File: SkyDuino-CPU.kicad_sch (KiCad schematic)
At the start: 35 parts, among them J11 USB-A RMT, J8 DBG, J9 USB_C Artisan, SW1 BOOT, U6 STM32F411RET6, U7 25MHz, U8 USBLC6-2SC6, U9 USBLC6-2SC6, Y1 32.768kHz

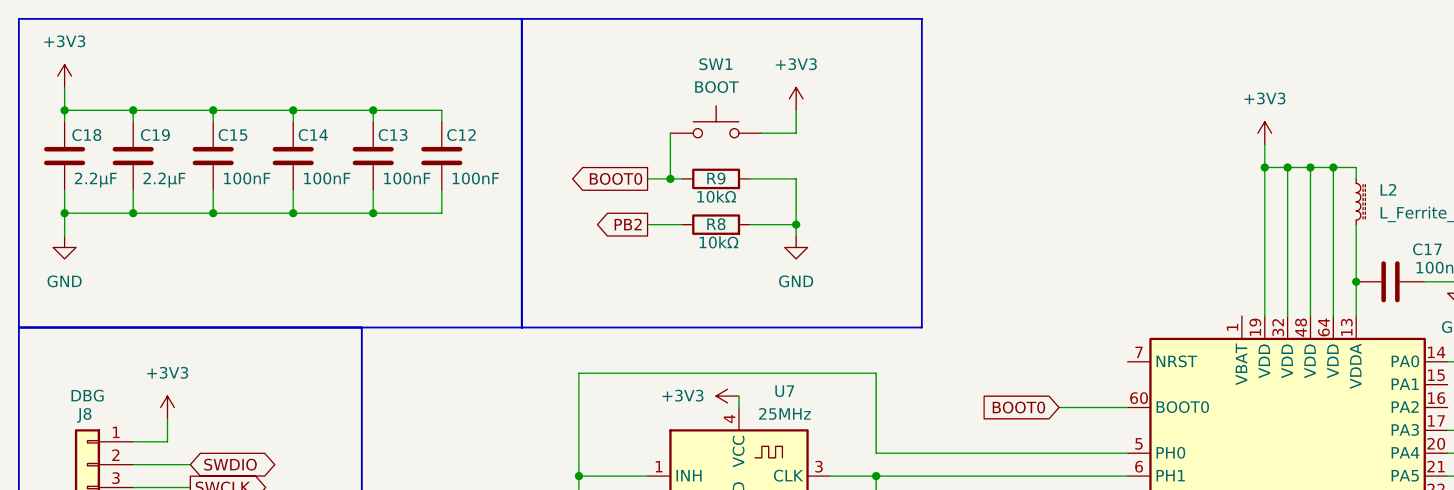
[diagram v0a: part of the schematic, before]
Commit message: Add VBat to VDD
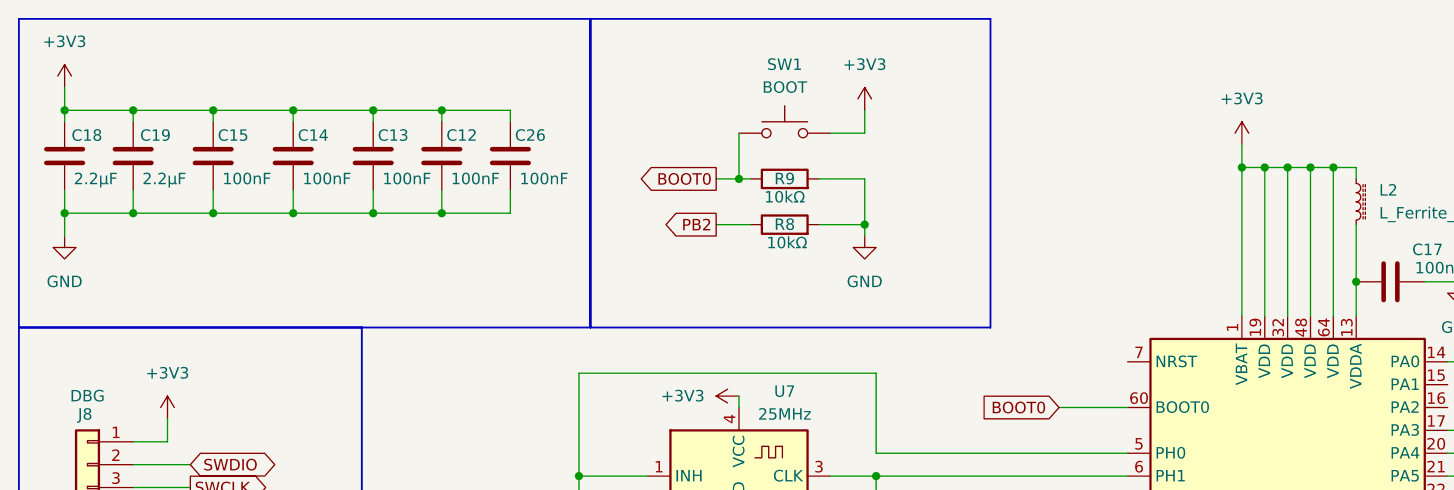
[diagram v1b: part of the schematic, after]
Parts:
- added C26: 100nF, Capacitor_SMD:C_0805_2012Metric_Pad1.18x1.45mm_HandSolder, symbol Device:C
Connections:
- net +3V3: now also U6.1 (VBAT), C26.1
- net GND: now also C26.2
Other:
- moved on the sheet: R8, R9, SW1

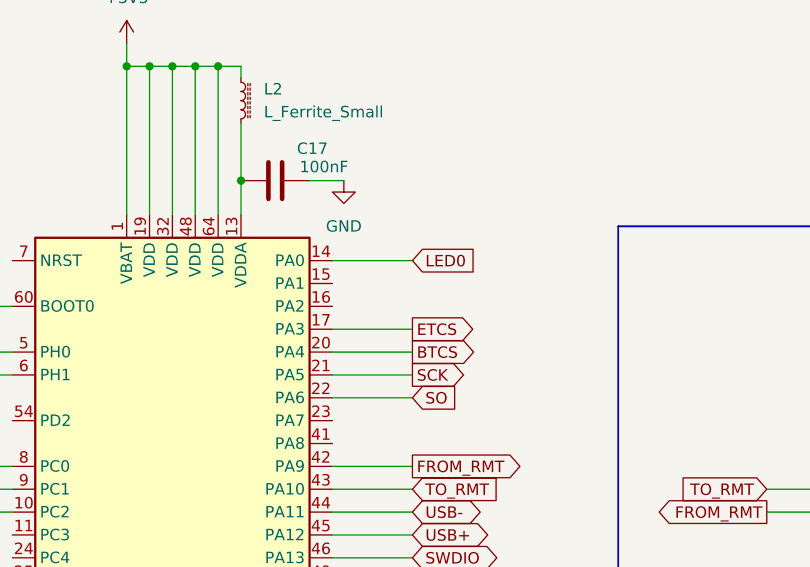
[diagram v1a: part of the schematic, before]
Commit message: Add NTC connection
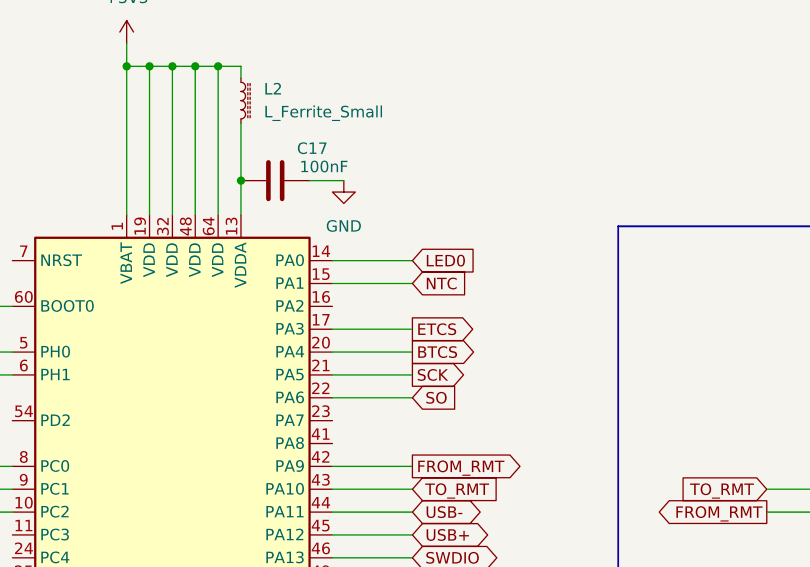
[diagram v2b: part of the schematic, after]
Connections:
- net NTC: now reaches U6.15 (PA1)
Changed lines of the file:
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@@
+	(wire
+		(pts
+			(xy 171.45 54.61) (xy 180.34 54.61)
+		)
+		(stroke
+			(width 0)
+			(type default)
+		)
+	)
 	(wire
 		(pts
@@
 				(hide yes)
 			)
+		)
+	)
+	(global_label "NTC"
+		(shape input)
+		(at 180.34 54.61 0)
+		(fields_autoplaced yes)
+		(effects
+			(font
+				(size 1.27 1.27)
+			)
+			(justify left)
+		)
+		(property "Intersheetrefs" "${INTERSHEET_REFS}"
+			(at 186.8933 54.61 0)
+			(effects
+				(font
+					(size 1.27 1.27)
+				)
+				(justify left)
+				(hide yes)
+			)

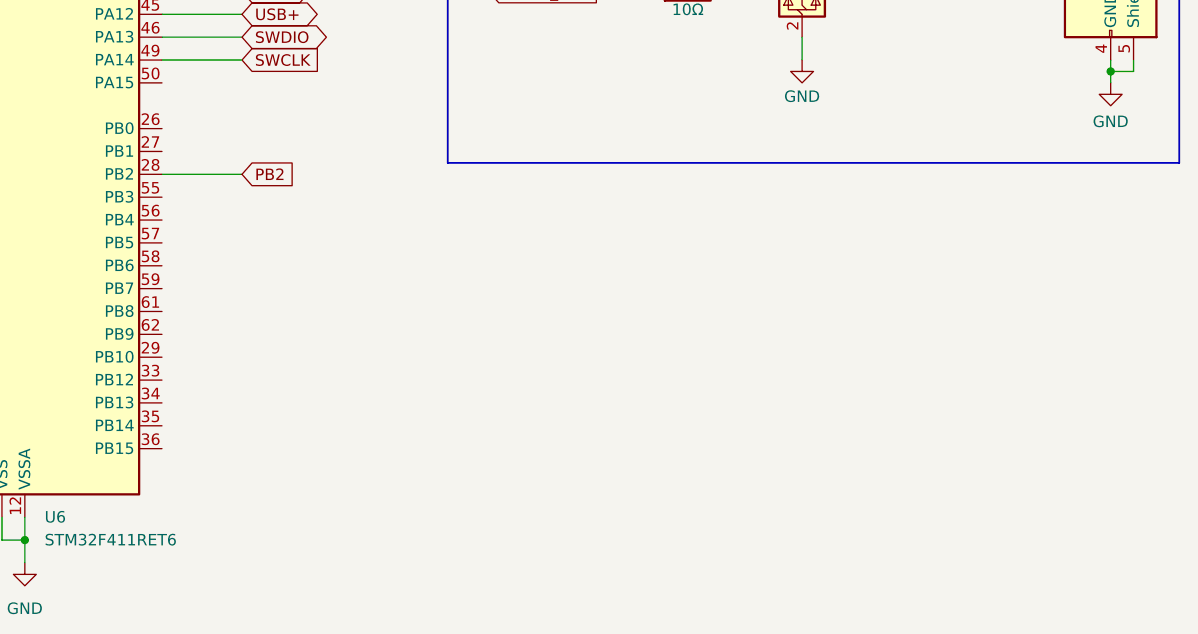
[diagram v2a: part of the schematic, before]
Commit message: Add I2C for the display
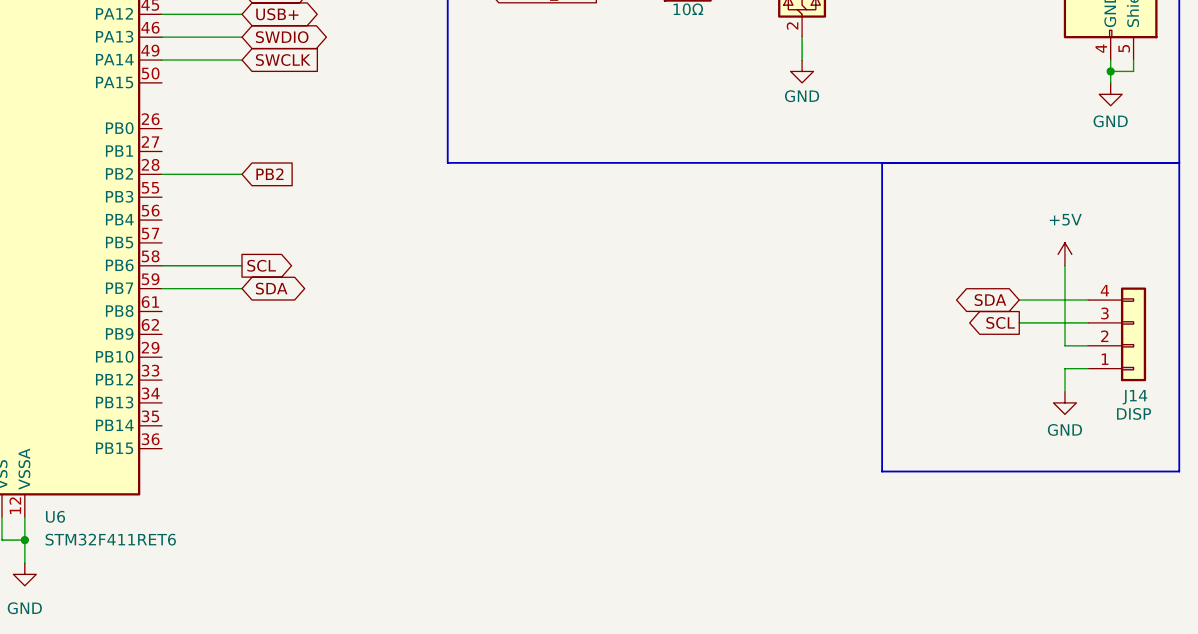
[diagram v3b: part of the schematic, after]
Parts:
- added J14: DISP, Connector_PinHeader_2.54mm:PinHeader_1x04_P2.54mm_Vertical, symbol Connector_Generic:Conn_01x04
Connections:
- net +5V: now also J14.2 (Pin_2)
- net GND: now also J14.1 (Pin_1)
- net SCL: now reaches U6.58 (PB6)
- net SCL: now also J14.3 (Pin_3)
- net SDA: now reaches U6.59 (PB7)
- net SDA: now also J14.4 (Pin_4)

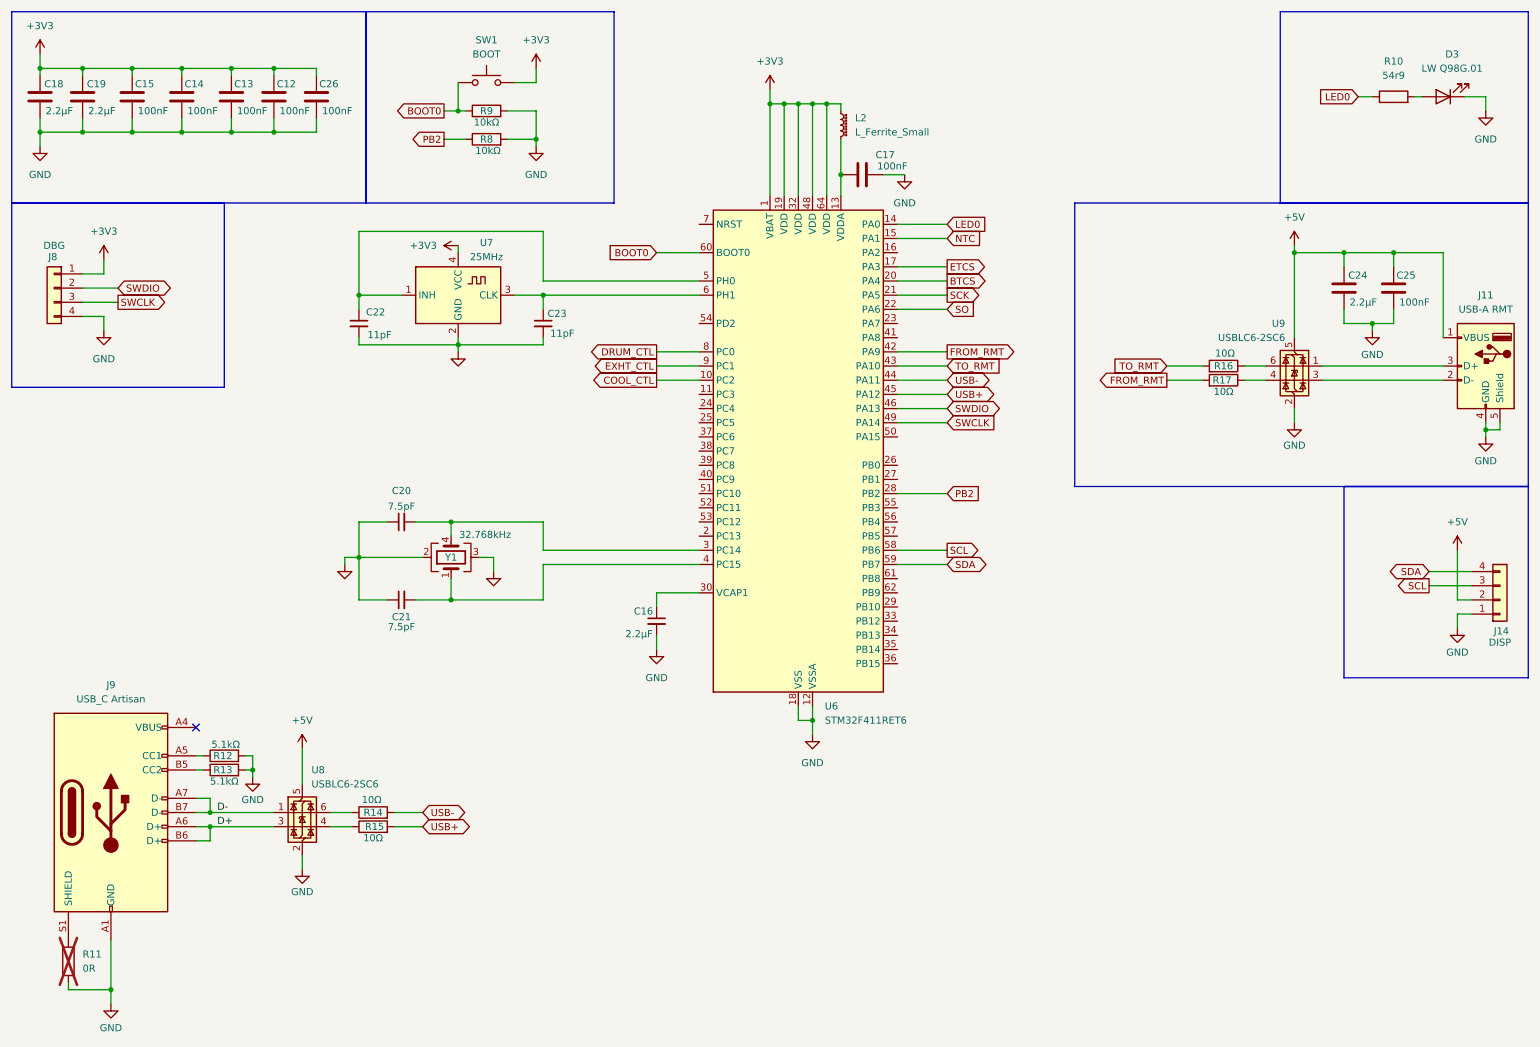
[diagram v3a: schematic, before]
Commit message: Re-annotate. Add NTC capacitor
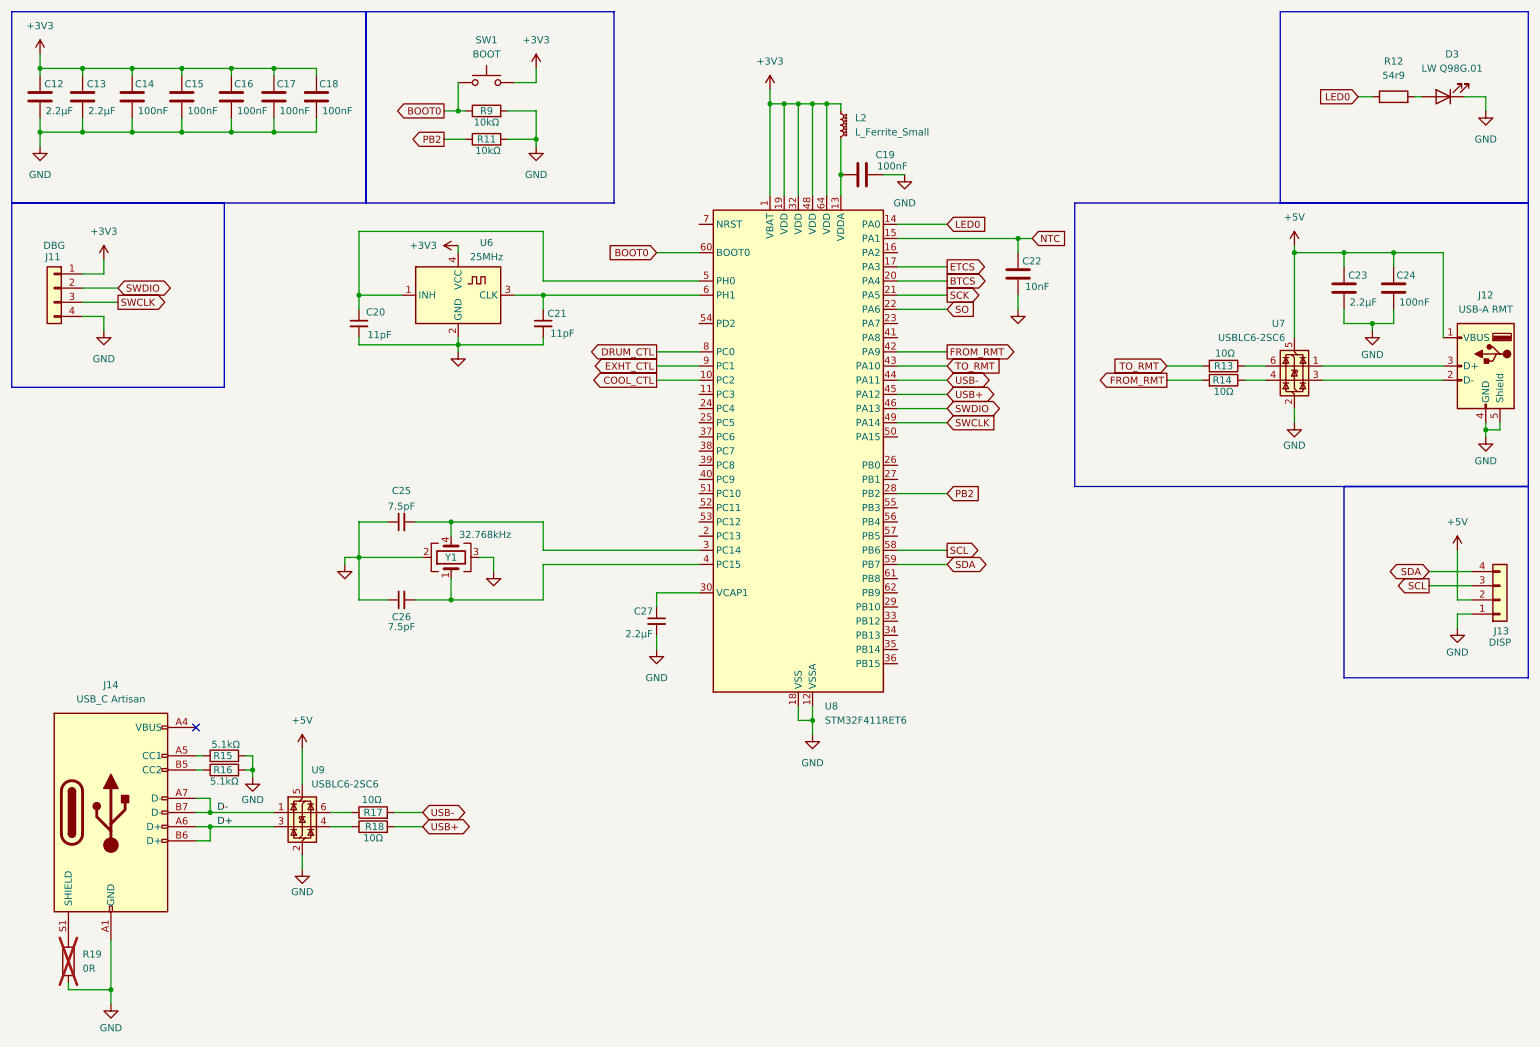
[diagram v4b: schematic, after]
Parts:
- added C22: 10nF, Capacitor_SMD:C_0805_2012Metric_Pad1.18x1.45mm_HandSolder, symbol Device:C
- renumbered C18 to C12, C19 to C13, C15 to C14, C14 to C15, C13 to C16, C12 to C17, C26 to C18, C17 to C19, C22 to C20, C23 to C21, C24 to C23, C25 to C24, C20 to C25, C21 to C26, C16 to C27, J8 to J11, J11 to J12, J14 to J13, J9 to J14, R8 to R11, R10 to R12, R16 to R13, R17 to R14, R12 to R15, R13 to R16, R14 to R17, R15 to R18, R11 to R19, U7 to U6, U9 to U7, U6 to U8, U8 to U9
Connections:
- net GND: now also C22.2
- net NTC: now also C22.1

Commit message: Add SSR
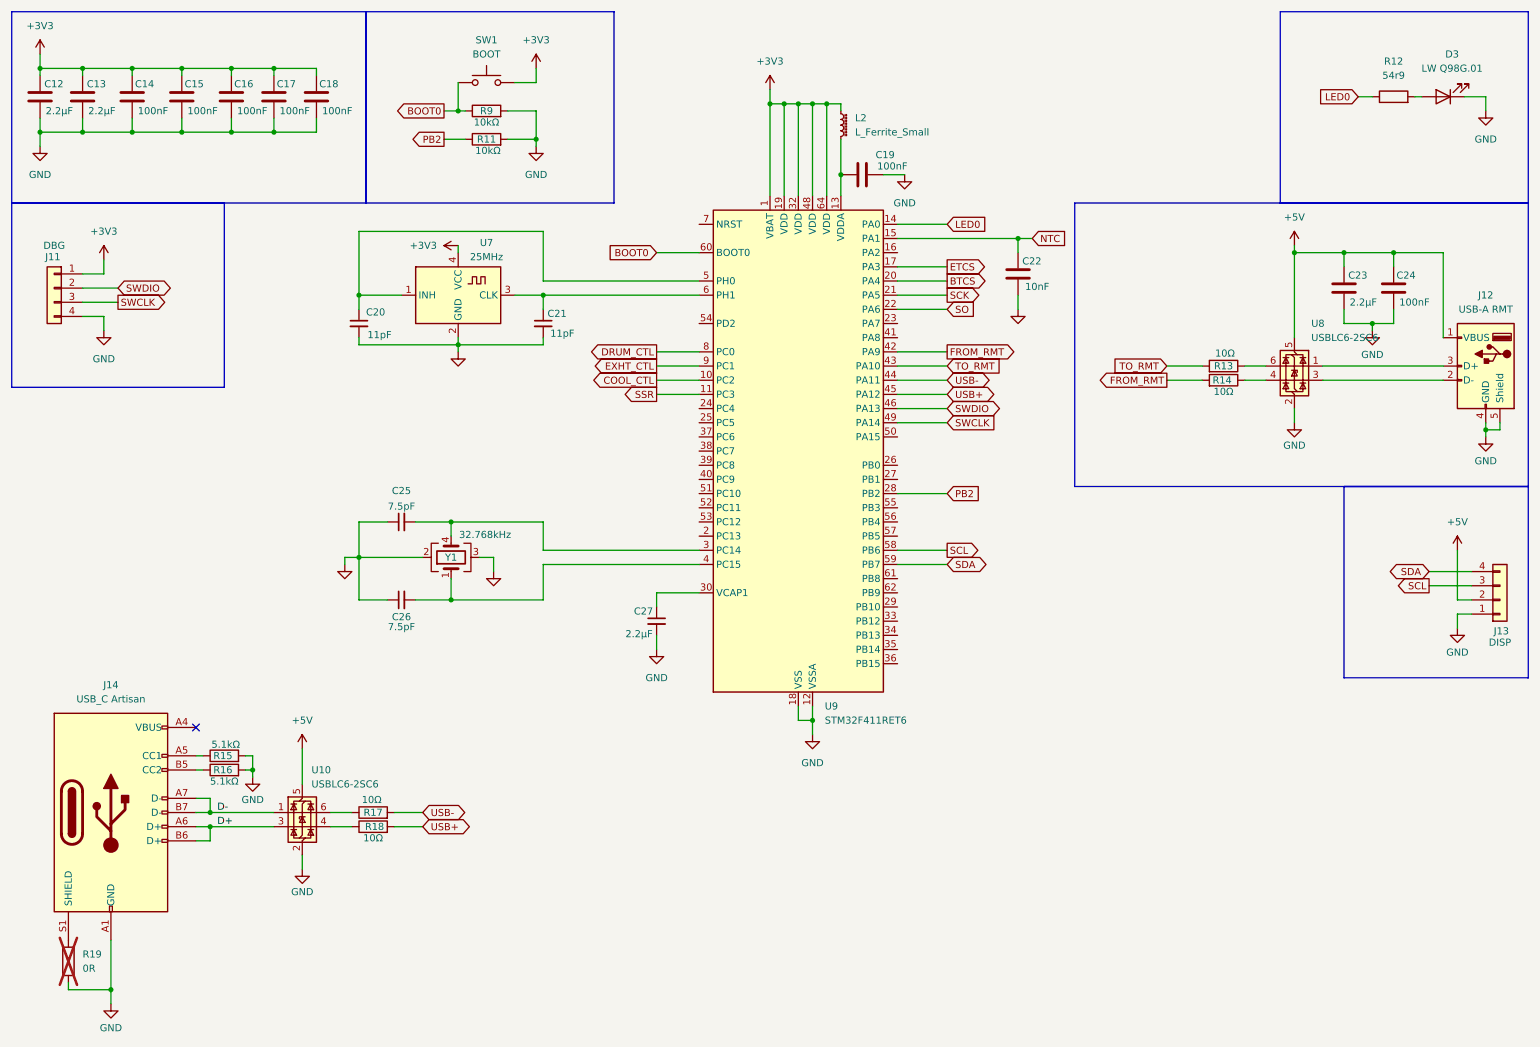
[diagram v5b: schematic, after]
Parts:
- renumbered U9 to U10, U6 to U7, U7 to U8, U8 to U9
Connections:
- net SSR: now reaches U9.11 (PC3)
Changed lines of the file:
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@@
 	(wire
 		(pts
+			(xy 128.27 82.55) (xy 135.89 82.55)
+		)
+		(stroke
+			(width 0)
+			(type default)
+		)
+	)
+	(wire
+		(pts
 			(xy 25.4 66.04) (xy 31.75 66.04)
 		)
@@
 		)
 	)
+	(global_label "SSR"
+		(shape output)
+		(at 128.27 82.55 180)
+		(fields_autoplaced yes)
+		(effects
+			(font
+				(size 1.27 1.27)
+			)
+			(justify right)
+		)
+		(property "Intersheetrefs" "${INTERSHEET_REFS}"
+			(at 121.5958 82.55 0)
+			(effects
+				(font
+					(size 1.27 1.27)
+				)
+				(justify right)
+				(hide yes)
+			)
+		)
+	)
 	(global_label "SWDIO"
 		(shape bidirectional)
@@
 		(on_board yes)
 		(dnp no)
-		(property "Reference" "U8"
+		(property "Reference" "U9"
 			(at 158.4041 138.43 0)
 			(effects
@@
 			(project "SkyDuino-Hardware"
 				(path "/a6671232-96de-4e23-ad68-f9378c1c0159/30f0c390-a08b-495d-a987-fe20b2c7c730"
-					(reference "U8")
+					(reference "U9")
 					(unit 1)
 				)
@@
 		(dnp no)
 		(fields_autoplaced yes)
-		(property "Reference" "U9"
+		(property "Reference" "U10"
 			(at 66.4211 149.86 0)
 			(effects
@@
 			(project "SkyDuino-Hardware"
 				(path "/a6671232-96de-4e23-ad68-f9378c1c0159/30f0c390-a08b-495d-a987-fe20b2c7c730"
-					(reference "U9")
+					(reference "U10")
 					(unit 1)
 				)
@@
 		(dnp no)
 		(fields_autoplaced yes)
-		(property "Reference" "U7"
-			(at 240.9189 69.85 0)
+		(property "Reference" "U8"
+			(at 245.5865 69.85 0)
 			(effects
 				(font
 					(size 1.27 1.27)
 				)
-				(justify left)
+				(justify right)
 			)
 		)
 		(property "Value" "USBLC6-2SC6"
-			(at 240.9189 72.39 0)
+			(at 245.5865 72.39 0)
 			(effects
 				(font
 					(size 1.27 1.27)
 				)
-				(justify left)
+				(justify right)
 			)
 		)
@@
 			(project "SkyDuino-Hardware"
 				(path "/a6671232-96de-4e23-ad68-f9378c1c0159/30f0c390-a08b-495d-a987-fe20b2c7c730"
-					(reference "U7")
+					(reference "U8")
 					(unit 1)
 				)
@@
 		(on_board yes)
 		(dnp no)
-		(property "Reference" "U6"
+		(property "Reference" "U7"
 			(at 97.79 55.372 0)
 			(effects
@@
 			(project "SkyDuino-Hardware"
 				(path "/a6671232-96de-4e23-ad68-f9378c1c0159/30f0c390-a08b-495d-a987-fe20b2c7c730"
-					(reference "U6")
+					(reference "U7")
 					(unit 1)
 				)

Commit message: Update footprints
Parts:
- Y1: footprint (none) -> Oscillators:Diodes Inc G43270021
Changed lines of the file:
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@@
 			)
 		)
-		(property "Footprint" ""
+		(property "Footprint" "Oscillators:Diodes Inc G43270021"
 			(at 91.44 111.76 0)
 			(effects
